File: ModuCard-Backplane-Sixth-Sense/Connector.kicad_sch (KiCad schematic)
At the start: 1 part, among them J17 09031967921

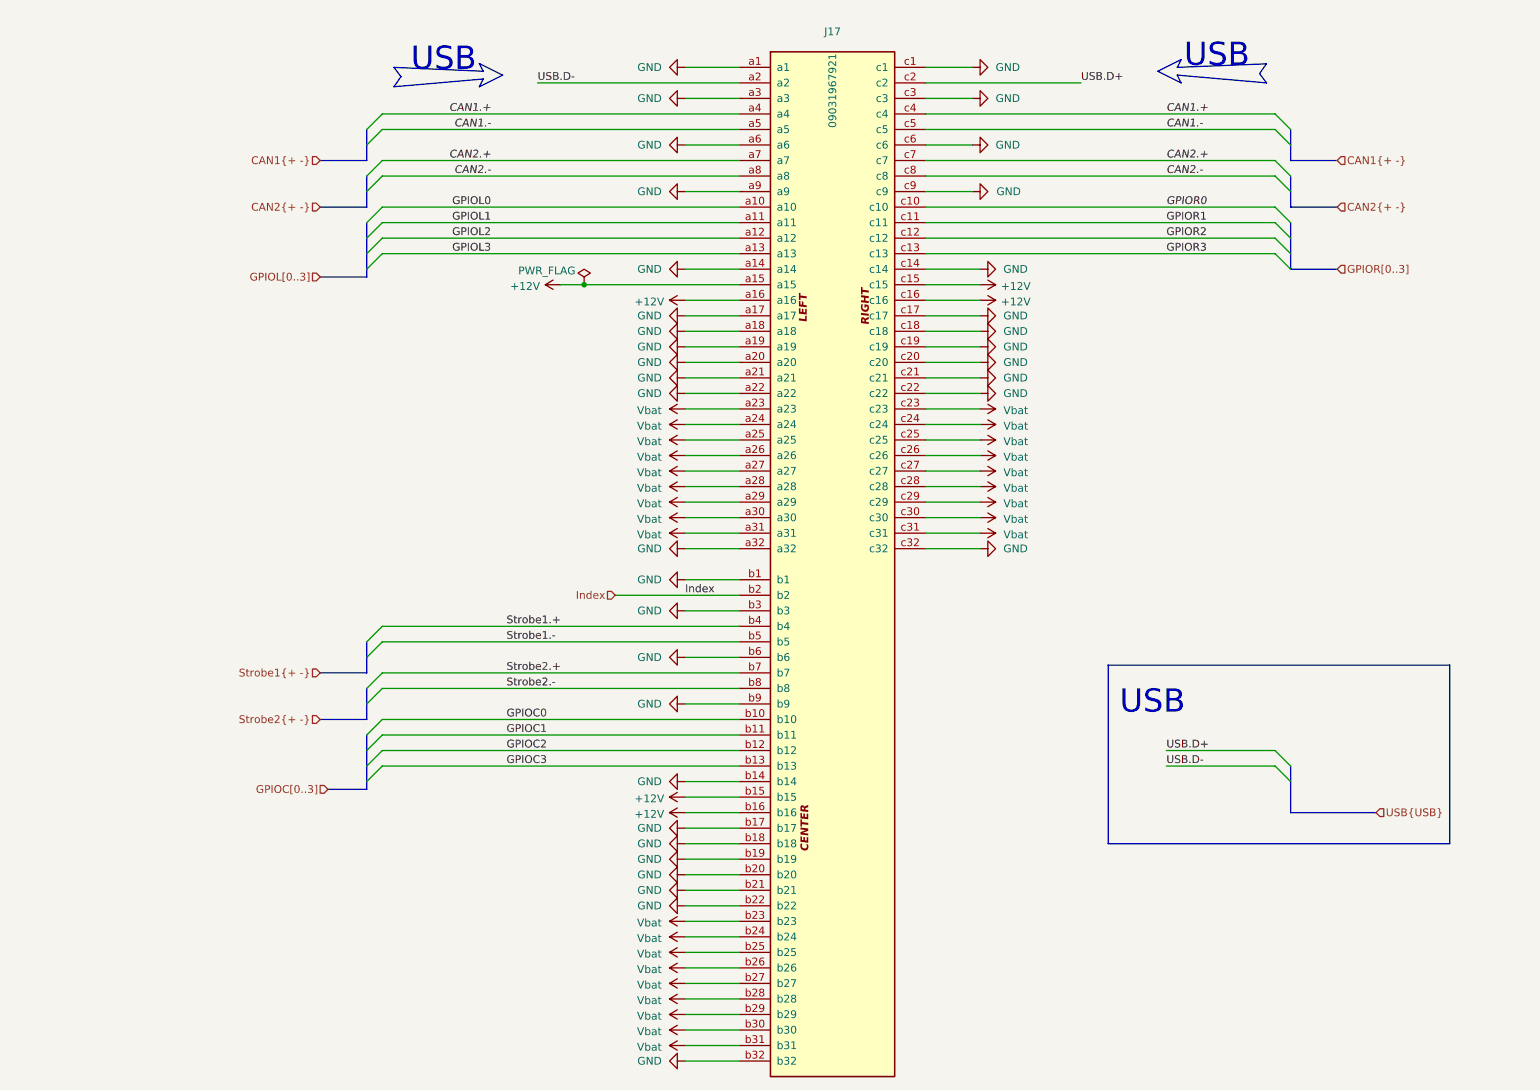
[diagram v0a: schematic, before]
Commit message: fix DRC errors, change pinout
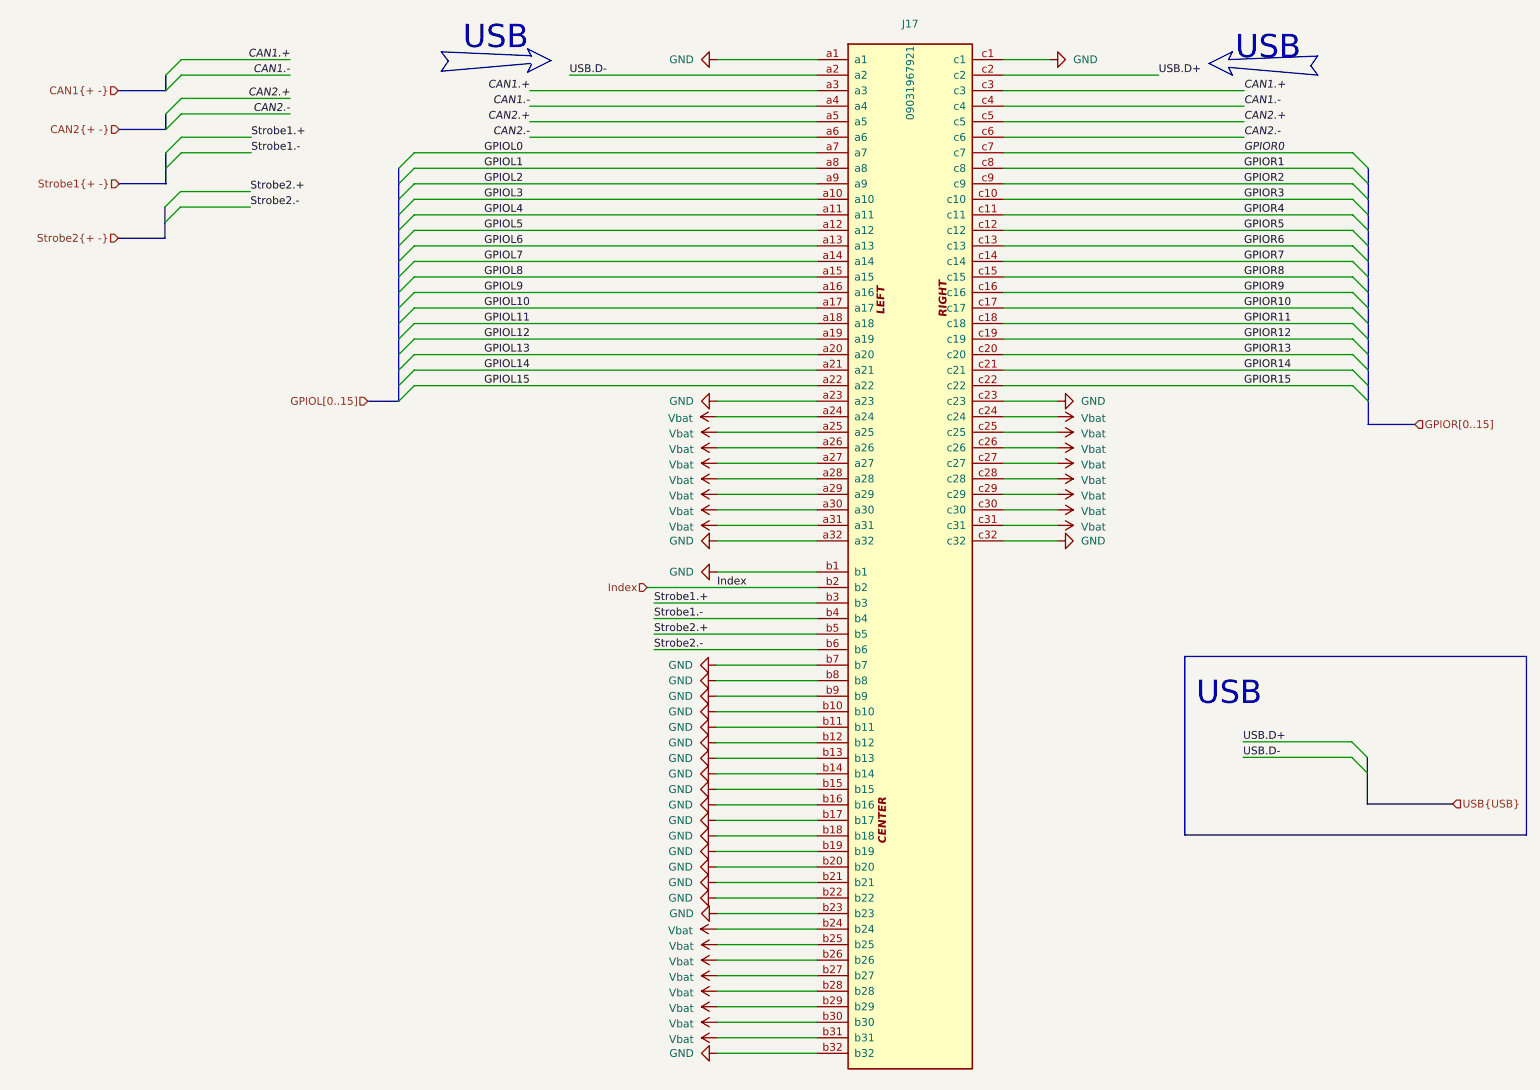
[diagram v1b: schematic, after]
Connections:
- net GPIOC0 is gone; now on net GND: J17.b10
- net GPIOC1 is gone; now on net GND: J17.b11
- net GPIOC2 is gone; now on net GND: J17.b12
- net GPIOC3 is gone; now on net GND: J17.b13
- net CAN1.+: now also J17.a3, J17.c3; no longer J17.a4, J17.c4
- net CAN1.-: now also J17.a4, J17.c4; no longer J17.a5, J17.c5
- net CAN2.+: now also J17.a5, J17.c5; no longer J17.a7, J17.c7
- net CAN2.-: now also J17.a6, J17.c6; no longer J17.a8, J17.c8
- net GND: now also J17.a23, J17.b15, J17.b16, J17.b23, J17.b7, J17.b8, J17.c23; no longer J17.a14, J17.a17, J17.a18, J17.a19, J17.a20, J17.a21, J17.a22, J17.a3, J17.a6, J17.a9, J17.b3, J17.b6, J17.c14, J17.c17, J17.c18, J17.c19, J17.c20, J17.c21, J17.c22, J17.c3, J17.c6, J17.c9
- net GPIOL0: now also J17.a7; no longer J17.a10
- net GPIOL1: now also J17.a8; no longer J17.a11
- net GPIOL2: now also J17.a9; no longer J17.a12
- net GPIOL3: now also J17.a10; no longer J17.a13
- net GPIOR0: now also J17.c7; no longer J17.c10
- net GPIOR1: now also J17.c8; no longer J17.c11
- net GPIOR2: now also J17.c9; no longer J17.c12
- net GPIOR3: now also J17.c10; no longer J17.c13
- net Strobe1.+: now also J17.b3; no longer J17.b4
- net Strobe1.-: now also J17.b4; no longer J17.b5
- net Strobe2.+: now also J17.b5; no longer J17.b7
- net Strobe2.-: now also J17.b6; no longer J17.b8
- net Vbat: no longer J17.a23, J17.b23, J17.c23
- removed net +12V: J17.a15, J17.a16, J17.b15, J17.b16, J17.c15, J17.c16
- new net GPIOL10: J17.a17
- new net GPIOL11: J17.a18
- new net GPIOL12: J17.a19
- new net GPIOL13: J17.a20
- new net GPIOL14: J17.a21
- new net GPIOL15: J17.a22
- new net GPIOL4: J17.a11
- new net GPIOL5: J17.a12
- new net GPIOL6: J17.a13
- new net GPIOL7: J17.a14
- new net GPIOL8: J17.a15
- new net GPIOL9: J17.a16
- new net GPIOR10: J17.c17
- new net GPIOR11: J17.c18
- new net GPIOR12: J17.c19
- new net GPIOR13: J17.c20
- new net GPIOR14: J17.c21
- new net GPIOR15: J17.c22
- new net GPIOR4: J17.c11
- new net GPIOR5: J17.c12
- new net GPIOR6: J17.c13
- new net GPIOR7: J17.c14
- new net GPIOR8: J17.c15
- new net GPIOR9: J17.c16
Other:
- moved on the sheet: J17

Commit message: project overhaul
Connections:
- net GND: no longer J17.b1
- net Index renamed Index2
- new net Index1: J17.b1
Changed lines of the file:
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@@
 	(wire
 		(pts
+			(xy 118.11 107.95) (xy 146.05 107.95)
+		)
+		(stroke
+			(width 0)
+			(type default)
+		)
+	)
+	(wire
+		(pts
 			(xy 129.54 161.29) (xy 146.05 161.29)
 		)
@@
 	(wire
 		(pts
-			(xy 129.6924 107.95) (xy 146.05 107.95)
-		)
-		(stroke
-			(width 0)
-			(type default)
-		)
-	)
-	(wire
-		(pts
 			(xy 80.1624 74.93) (xy 146.05 74.93)
 		)
@@
 		)
 	)
-	(label "Index"
-		(at 129.6924 110.49 0)
+	(label "Index2"
+		(at 119.38 110.49 0)
 		(effects
 			(font
@@
 		)
 	)
+	(label "Index1"
+		(at 119.2276 107.95 0)
+		(effects
+			(font
+				(size 1.27 1.27)
+			)
+			(justify left bottom)
+		)
+	)
 	(label "CAN2.+"
 		(at 215.9 34.29 0)
@@
 		)
 	)
-	(hierarchical_label "Index"
-		(shape input)
+	(hierarchical_label "Index2"
+		(shape bidirectional)
 		(at 118.2624 110.49 180)
 		(effects
@@
 		)
 	)
+	(hierarchical_label "Index1"
+		(shape bidirectional)
+		(at 118.11 107.95 180)
+		(effects
+			(font
+				(size 1.27 1.27)
+			)
+			(justify right)
+		)
+	)
 	(hierarchical_label "Strobe2{+ -}"
 		(shape input)
@@
 					(unit 1)
 				)
-			)
-		)
-	)
-	(symbol
-		(lib_id "power:GND")
-		(at 129.6924 107.95 270)
-		(unit 1)
-		(body_style 1)
-		(exclude_from_sim no)
-		(in_bom yes)
-		(on_board yes)
-		(in_pos_files yes)
-		(dnp no)
-		(fields_autoplaced yes)
-		(property "Reference" "#PWR0192"
-			(at 123.3424 107.95 0)
-			(hide yes)
-			(show_name no)
-			(do_not_autoplace no)
-			(effects
-				(font
-					(size 1.27 1.27)
-				)
-			)
-		)
-		(property "Value" "GND"
-			(at 125.8824 107.9499 90)
-			(show_name no)
-			(do_not_autoplace no)
-			(effects
-				(font
-					(size 1.27 1.27)
-				)
-				(justify right)
-			)
-		)
-		(property "Footprint" ""
-			(at 129.6924 107.95 0)
-			(hide yes)
-			(show_name no)
-			(do_not_autoplace no)
-			(effects
-				(font
-					(size 1.27 1.27)
-				)
-			)
-		)
-		(property "Datasheet" ""
-			(at 129.6924 107.95 0)
-			(hide yes)
-			(show_name no)
-			(do_not_autoplace no)
-			(effects
-				(font
-					(size 1.27 1.27)
-				)
-			)
-		)
-		(property "Description" "Power symbol creates a global label with name \"GND\" , ground"
-			(at 129.6924 107.95 0)
-			(hide yes)
-			(show_name no)
-			(do_not_autoplace no)
-			(effects
-				(font
-					(size 1.27 1.27)
-				)
-			)
-		)
-		(pin "1"
-		)
-		(instances
-			(project "ModuCard-Backplane-Sixth-Sense"
-				(path "/b8e6d233-63ab-459d-a617-f62d9ba23c71/19d333a2-f22e-4eca-9572-c6d456152e84"
-					(reference "#PWR0192")
-					(unit 1)
-				)
-				(path "/b8e6d233-63ab-459d-a617-f62d9ba23c71/786eaee9-ca46-4374-8031-46bd7bfc8cd1"
-					(reference "#PWR0194")
-					(unit 1)
-				)
-				(path "/b8e6d233-63ab-459d-a617-f62d9ba23c71/844a7d3a-2f28-4b70-a317-bd0b8d4e14ec"
-					(reference "#PWR0202")
-					(unit 1)
-				)
-				(path "/b8e6d233-63ab-459d-a617-f62d9ba23c71/c64324c9-a349-4e68-9d18-c46bf62fbd2c"
-					(reference "#PWR0200")
-					(unit 1)
-				)
-				(path "/b8e6d233-63ab-459d-a617-f62d9ba23c71/c8b1d21f-a391-43a1-b71c-f7309df0bf6f"
-					(reference "#PWR0196")
-					(unit 1)
-				)
-				(path "/b8e6d233-63ab-459d-a617-f62d9ba23c71/ca0552b9-49fb-41b8-a9ee-d117cb5c8971"
-					(reference "#PWR0198")
-					(unit 1)
-				)
